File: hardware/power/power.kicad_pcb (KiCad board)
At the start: 2 copper layers, 37 x 41 mm, 30 parts, among them J1 SF6, J2 SF6, J3 PinHeader2x4, J4 PinHeader2x4, J5 PinHeader2x4, J6 SF6, J7 SF6, J8 SF6, Q1 ISC022N10NM6, Q2 ISC022N10NM6, Q3 ISC022N10NM6, Q4 ISC022N10NM6, Q5 ISC022N10NM6, Q6 ISC022N10NM6

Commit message: intermediate commit, some changes needed before first purchase
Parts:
- removed H1, H2, H3, H4: HoleM3_ISO14580, MountingHole:MountingHole_3.2mm_M3_ISO14580
- removed Q1, Q2, Q3, Q4, Q5, Q6: ISC022N10NM6, Package_SO:PowerPAK_SO-8_Single
- removed R2, R3, R4, R5, R6: 500u, Resistor_SMD:R_Shunt_Vishay_WSKW0612
- removed TH1, TH2, TH3: NTC 10k, Resistor_SMD:R_0402_1005Metric
- added H101: HoleM2_ISO14580, MountingHole:MountingHole_2.2mm_M2_ISO14580, F.Cu at (116.0, 42.0)
- added H102: HoleM2_ISO14580, MountingHole:MountingHole_2.2mm_M2_ISO14580, F.Cu at (89.0, 84.0)
- added H103: HoleM2_ISO14580, MountingHole:MountingHole_2.2mm_M2_ISO14580, F.Cu at (89.0, 42.0)
- added H104: HoleM2_ISO14580, MountingHole:MountingHole_2.2mm_M2_ISO14580, F.Cu at (116.0, 84.0)
- added J109: SF6, Connector_Wire:SolderWirePad_1x01_SMD_3x6mm, F.Cu at (116.0, 69.0)
- added J110: SF6, Connector_Wire:SolderWirePad_1x01_SMD_3x6mm, F.Cu at (89.0, 69.0)
- added J111: PinHeader2x2, Connector_PinHeader_1.00mm:PinHeader_2x02_P1.00mm_Vertical_SMD, F.Cu at (95.0, 83.5)
- added Q201: ISC022N10NM6, mcrmv:PowerPAK_SO-8_Single, F.Cu at (110.0, 43.5)
- added Q202: ISC022N10NM6, mcrmv:PowerPAK_SO-8_Single, F.Cu at (96.5, 43.5)
- added Q203: ISC022N10NM6, mcrmv:PowerPAK_SO-8_Single, F.Cu at (110.0, 58.5)
- added Q204: ISC022N10NM6, mcrmv:PowerPAK_SO-8_Single, F.Cu at (96.5, 58.5)
- added Q205: ISC022N10NM6, mcrmv:PowerPAK_SO-8_Single, F.Cu at (110.0, 73.5)
- added Q206: ISC022N10NM6, mcrmv:PowerPAK_SO-8_Single, F.Cu at (96.5, 73.5)
- added Q301: ISC022N10NM6, mcrmv:PowerPAK_SO-8_Single, F.Cu at (110.0, 49.0)
- added Q302: ISC022N10NM6, mcrmv:PowerPAK_SO-8_Single, F.Cu at (96.5, 49.0)
- added Q303: ISC022N10NM6, mcrmv:PowerPAK_SO-8_Single, F.Cu at (110.0, 64.0)
- added Q304: ISC022N10NM6, mcrmv:PowerPAK_SO-8_Single, F.Cu at (96.5, 64.0)
- added Q305: ISC022N10NM6, mcrmv:PowerPAK_SO-8_Single, F.Cu at (110.0, 79.0)
- added Q306: ISC022N10NM6, mcrmv:PowerPAK_SO-8_Single, F.Cu at (96.5, 79.0)
- added R102: 200u, mcrmv:WSK1216, F.Cu at (104.0, 64.5)
- added R103: 200u, mcrmv:WSK1216, F.Cu at (104.0, 79.5)
- added REF**: OSHW-Logo_5.7x6mm_SilkScreen, Symbol:OSHW-Logo_5.7x6mm_SilkScreen, F.Cu at (102.5, 74.0)
- added TH101: NTC 10k, Resistor_SMD:R_0402_1005Metric, F.Cu at (91.8, 80.1)
- J103: renamed from J3; value PinHeader2x4 -> PinHeader2x2; footprint Connector_PinHeader_1.00mm:PinHeader_2x04_P1.00mm_Vertical_SMD -> Connector_PinHeader_1.00mm:PinHeader_2x02_P1.00mm_Vertical_SMD
- J104: renamed from J4; value PinHeader2x4 -> PinHeader2x2; footprint Connector_PinHeader_1.00mm:PinHeader_2x04_P1.00mm_Vertical_SMD -> Connector_PinHeader_1.00mm:PinHeader_2x02_P1.00mm_Vertical_SMD
- J105: renamed from J5; value PinHeader2x4 -> PinHeader2x2; footprint Connector_PinHeader_1.00mm:PinHeader_2x04_P1.00mm_Vertical_SMD -> Connector_PinHeader_1.00mm:PinHeader_2x02_P1.00mm_Vertical_SMD
- R101: renamed from R1; value 500u -> 200u; footprint Resistor_SMD:R_Shunt_Vishay_WSKW0612 -> mcrmv:WSK1216
- moved FID101 33.7 mm to (116.5, 45.5)
- moved FID102 29.7 mm to (88.5, 80.0)
- moved FID103 22.6 mm to (102.0, 41.5)
- moved J106 12.1 mm to (102.0, 53.5)
- moved R101 12.0 mm to (104.0, 49.5), turned to 180 degrees
- moved J107 9.92 mm to (102.0, 68.5)
- moved J103 9.55 mm to (109.0, 53.5)
- moved J108 8.32 mm to (102.0, 83.4)
- moved J104 6.58 mm to (109.0, 68.5)
- moved J101 6.05 mm to (116.0, 53.0), turned to 180 degrees
- moved J102 6.05 mm to (89.0, 53.0), turned to 180 degrees
- moved J105 3.64 mm to (109.0, 83.5)
- renumbered FID1 to FID101, FID2 to FID102, FID3 to FID103, J1 to J101, J2 to J102, J6 to J106, J7 to J107, J8 to J108
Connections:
- J103 pad 1: /P1 -> /S1_P
- J103 pad 3: /S1_P -> /S1_N
- J103 pad 4: /NTC1+ -> /GL1
- J104 pad 1: /P2 -> /S2_P
- J104 pad 3: /S2_P -> /S2_N
- J104 pad 4: /NTC2+ -> /GL2
- J105 pad 1: /P3 -> /S3_P
- J105 pad 3: /S3_P -> /S3_N
- J105 pad 4: /NTC3+ -> /GL3
- R101 pad 1: /P1 -> /P1_TAB
- R101 pad 2: /S1_P -> /S1_N
- R101 pad 3: /S1_N -> /S1_P
- R101 pad 4: /P1_TAB -> /P1
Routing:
- net GND: track 91.1 -> 0.00 mm
- net /P1: track 6.19 -> 0.00 mm
- net /P2: track 5.96 -> 0.00 mm
- net /P3: track 5.88 -> 0.00 mm
- net /GH1: track 6.11 -> 11.6 mm
- net /GH3: track 6.11 -> 11.6 mm
- net /GH2: track 6.08 -> 11.5 mm
- net /NTC3+: track 4.44 -> 0.00 mm
- net /NTC2+: track 4.44 -> 0.00 mm
- net /NTC2-: track 4.25 -> 0.00 mm
- net /NTC3-: track 4.14 -> 0.00 mm
- net /GL1: track 23.8 -> 27.9 mm
- net /GL3: track 23.9 -> 27.8 mm
- net /GL2: track 23.8 -> 27.7 mm
- net /NTC1-: track 3.43 -> 0.00 mm
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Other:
- board size 37 x 41 mm -> 31 x 46 mm
- board text added: "${TITLE} ${SUBTITLE} 2025"
- board text removed: "${TITLE} ${SUBTITLE} v${REV}"

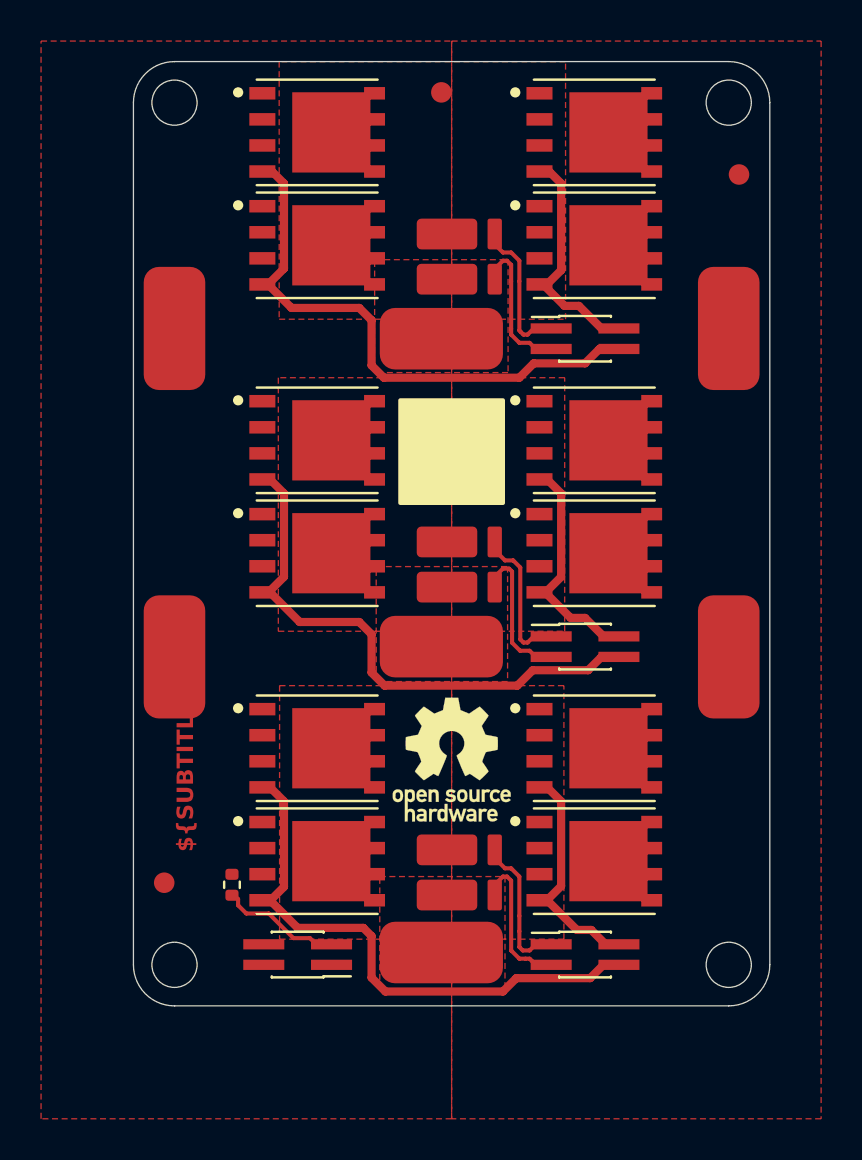
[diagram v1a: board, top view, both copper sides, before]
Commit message: added connectors to add individual current paths, filled with ntcs, plotted pdf, updated screenshots
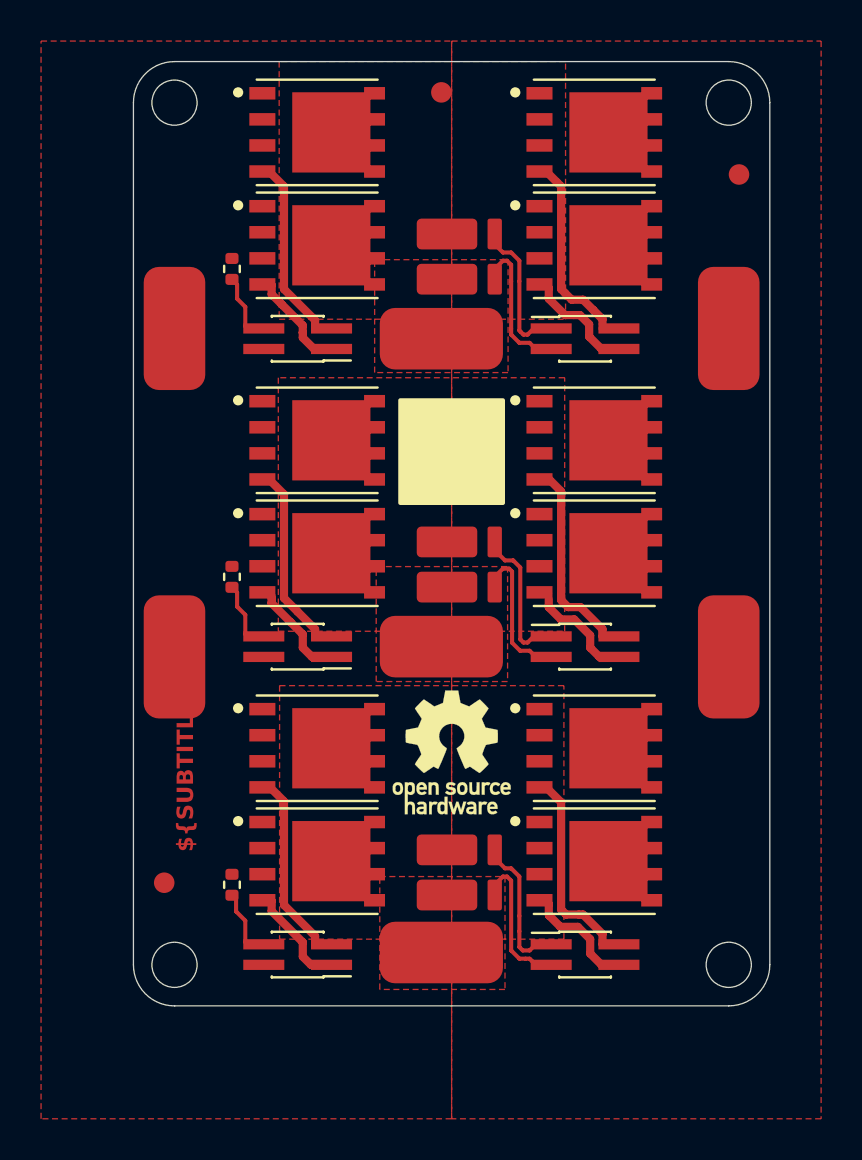
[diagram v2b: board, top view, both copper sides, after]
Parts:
- added J106: PinHeader2x2, Connector_PinHeader_1.00mm:PinHeader_2x02_P1.00mm_Vertical_SMD, F.Cu at (95.0, 53.5)
- added J107: PinHeader2x2, Connector_PinHeader_1.00mm:PinHeader_2x02_P1.00mm_Vertical_SMD, F.Cu at (95.0, 68.5)
- added TH102: NTC 10k, Resistor_SMD:R_0402_1005Metric, F.Cu at (91.8, 65.1)
- added TH103: NTC 10k, Resistor_SMD:R_0402_1005Metric, F.Cu at (91.8, 80.1)
- moved TH101 30.0 mm to (91.8, 50.1)
- moved REF** 0.35 mm to (102.5, 73.7)
- renumbered J111 to J108, J106 to J111, J107 to J112, J108 to J113
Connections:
- J103 pad 2: /GH1 -> /GH_P1_1
- J103 pad 4: /GL1 -> /GH_P1_2
- J104 pad 2: /GH2 -> /GH_P2_1
- J104 pad 4: /GL2 -> /GH_P2_2
- J105 pad 2: /GH3 -> /GH_P3_1
- J105 pad 4: /GL3 -> /GH_P3_2
- J108 pad 1: GND -> /GL_P3_2
- J108 pad 3: /NTC1+ -> /GL_P3_1
- J108 pad 4: GND -> /NTC3+
- Q201 pad 4: /GH1 -> /GH_P1_1
- Q202 pad 4: /GL1 -> /GL_P1_1
- Q203 pad 4: /GH2 -> /GH_P2_1
- Q204 pad 4: /GL2 -> /GL_P2_1
- Q205 pad 4: /GH3 -> /GH_P3_1
- Q206 pad 4: /GL3 -> /GL_P3_1
- Q301 pad 4: /GH1 -> /GH_P1_2
- Q302 pad 4: /GL1 -> /GL_P1_2
- Q303 pad 4: /GH2 -> /GH_P2_2
- Q304 pad 4: /GL2 -> /GL_P2_2
- Q305 pad 4: /GH3 -> /GH_P3_2
- Q306 pad 4: /GL3 -> /GL_P3_2
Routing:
- net /GL1: track 27.9 -> 0.00 mm
- net /GL3: track 27.8 -> 0.00 mm
- net /GL2: track 27.7 -> 0.00 mm
- net /GH1: track 11.6 -> 0.00 mm
- net /GH3: track 11.6 -> 0.00 mm
- net /GH2: track 11.5 -> 0.00 mm
- net /GH_P1_1: track 0.00 -> 10.5 mm
- net /GH_P3_1: track 0.00 -> 10.4 mm
- net /GH_P2_1: track 0.00 -> 10.3 mm
- net /GL_P3_1: track 0.00 -> 9.73 mm
- net /GL_P1_1: track 0.00 -> 9.67 mm
- net /GL_P2_1: track 0.00 -> 9.67 mm
- net /GH_P3_2: track 0.00 -> 5.90 mm
- net /GH_P1_2: track 0.00 -> 5.83 mm
- net /GH_P2_2: track 0.00 -> 5.59 mm
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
